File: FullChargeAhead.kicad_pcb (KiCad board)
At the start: 2 copper layers, 27.2 x 15.2 mm, 13 parts, among them P1 USB_PWR, P2 BATT, U1 MCP73834-FCI/UN

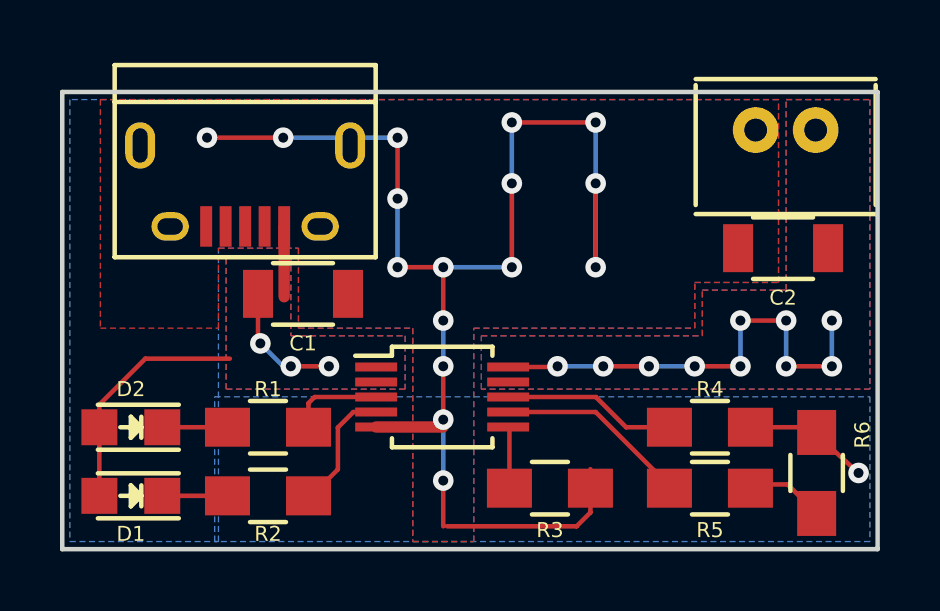
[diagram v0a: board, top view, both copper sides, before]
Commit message: Fix USB footprint.
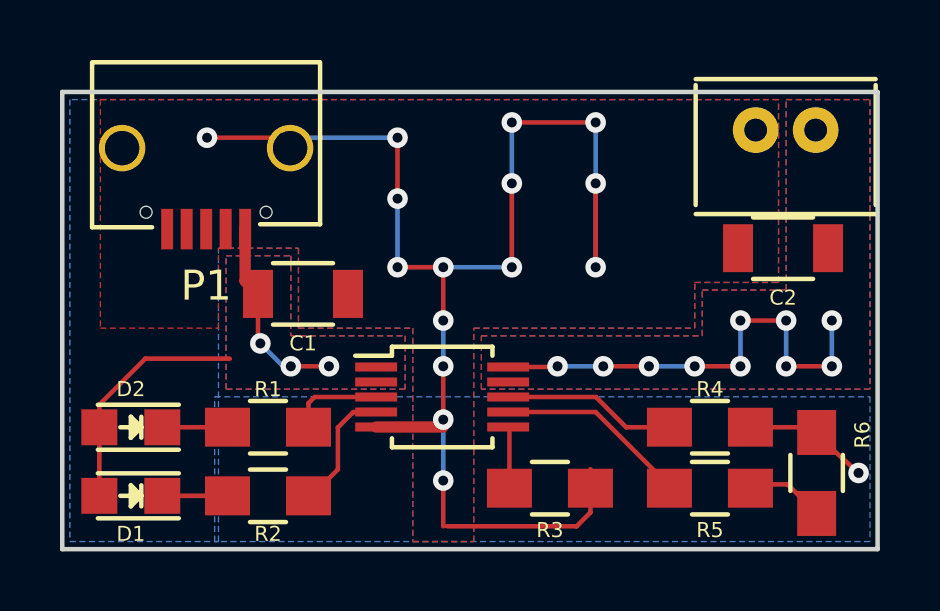
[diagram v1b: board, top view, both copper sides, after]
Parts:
- P1: footprint Connect:USB_Micro-B -> gl:USB_Micro-B-ebay
- moved P1 2.63 mm to (153.4, 104.5)
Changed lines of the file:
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@@
-(kicad_pcb (version 4) (host pcbnew 4.0.2+e4-6225~38~ubuntu16.04.1-stable)
+(kicad_pcb (version 4) (host pcbnew 4.0.3+e1-6302~38~ubuntu16.04.1-stable)
   (general
-    (links 27)
-    (no_connects 0)
+    (links 25)
+    (no_connects 3)
     (area 148.514999 99.238999 175.843001 114.629001)
     (thickness 1.6)
     (drawings 6)
-    (tracks 98)
+    (tracks 99)
     (zones 0)
     (modules 13)
@@
   )
   (setup
-    (last_trace_width 0.1524)
+    (last_trace_width 0.381)
     (user_trace_width 0.1524)
     (user_trace_width 0.381)
@@
     (pad_to_mask_clearance 0.2)
     (aux_axis_origin 0 0)
-    (visible_elements FFFEFF7F)
+    (visible_elements FFFFFF7F)
     (pcbplotparams
       (layerselection 0x00030_80000001)
@@
       (effects (font (size 0.5 0.5) (thickness 0.125)))
     )
-    (fp_text value 4.7u (at 0 2.3) (layer F.Fab)
+    (fp_text value 4.7u (at 0 0) (layer F.Fab)
       (effects (font (size 1 1) (thickness 0.15)))
     )
@@
       (effects (font (size 0.5 0.5) (thickness 0.125)))
     )
-    (fp_text value 4.7u (at 0 2.3 180) (layer F.Fab)
+    (fp_text value 4.7u (at -0.103 -0.127 180) (layer F.Fab)
       (effects (font (size 1 1) (thickness 0.15)))
     )
@@
       (effects (font (size 0.5 0.5) (thickness 0.125)))
     )
-    (fp_text value LED (at 0 1.75 180) (layer F.Fab)
+    (fp_text value LED (at 0 1.75 180) (layer F.Fab) hide
       (effects (font (size 1 1) (thickness 0.15)))
     )
@@
       (effects (font (size 0.5 0.5) (thickness 0.125)))
     )
-    (fp_text value LED (at 0 1.75 180) (layer F.Fab)
+    (fp_text value LED (at 0 1.75 180) (layer F.Fab) hide
       (effects (font (size 1 1) (thickness 0.15)))
     )
@@
     )
   )
-  (module Connect:USB_Micro-B (layer F.Cu)
-    (at 154.686 102.235 180)
-    (descr "Micro USB Type B Receptacle")
-    (tags "USB USB_B USB_micro USB_OTG")
-    (attr smd)
-    (fp_text reference P1 (at 2.032 -3.683 180) (layer F.SilkS) hide
-      (effects (font (size 1 1) (thickness 0.15)))
-    )
-    (fp_text value USB_PWR (at 0 4.8 180) (layer F.Fab)
-      (effects (font (size 1 1) (thickness 0.15)))
-    )
-    (fp_line (start -4.6 -2.8) (end 4.6 -2.8) (layer F.CrtYd) (width 0.05))
-    (fp_line (start 4.6 -2.8) (end 4.6 4.05) (layer F.CrtYd) (width 0.05))
-    (fp_line (start 4.6 4.05) (end -4.6 4.05) (layer F.CrtYd) (width 0.05))
-    (fp_line (start -4.6 4.05) (end -4.6 -2.8) (layer F.CrtYd) (width 0.05))
-    (fp_line (start -4.3509 3.81746) (end 4.3491 3.81746) (layer F.SilkS) (width 0.15))
-    (fp_line (start -4.3509 -2.58754) (end 4.3491 -2.58754) (layer F.SilkS) (width 0.15))
-    (fp_line (start 4.3491 -2.58754) (end 4.3491 3.81746) (layer F.SilkS) (width 0.15))
-    (fp_line (start 4.3491 2.58746) (end -4.3509 2.58746) (layer F.SilkS) (width 0.15))
-    (fp_line (start -4.3509 3.81746) (end -4.3509 -2.58754) (layer F.SilkS) (width 0.15))
-    (pad 1 smd rect (at -1.3009 -1.56254 270) (size 1.35 0.4) (layers F.Cu F.Paste F.Mask)
-      (net 12 /Vin))
-    (pad 2 smd rect (at -0.6509 -1.56254 270) (size 1.35 0.4) (layers F.Cu F.Paste F.Mask)
-      (net 4 "Net-(P1-Pad2)"))
-    (pad 3 smd rect (at -0.0009 -1.56254 270) (size 1.35 0.4) (layers F.Cu F.Paste F.Mask)
-      (net 5 "Net-(P1-Pad3)"))
-    (pad 4 smd rect (at 0.6491 -1.56254 270) (size 1.35 0.4) (layers F.Cu F.Paste F.Mask)
-      (net 6 "Net-(P1-Pad4)"))
-    (pad 5 smd rect (at 1.2991 -1.56254 270) (size 1.35 0.4) (layers F.Cu F.Paste F.Mask)
-      (net 1 GND))
-    (pad 6 thru_hole oval (at -2.5009 -1.56254 270) (size 0.95 1.25) (drill oval 0.55 0.85) (layers *.Cu *.Mask F.SilkS)
-      (net 1 GND))
-    (pad 6 thru_hole oval (at 2.4991 -1.56254 270) (size 0.95 1.25) (drill oval 0.55 0.85) (layers *.Cu *.Mask F.SilkS)
-      (net 1 GND))
-    (pad 6 thru_hole oval (at -3.5009 1.13746 270) (size 1.55 1) (drill oval 1.15 0.5) (layers *.Cu *.Mask F.SilkS)
-      (net 1 GND))
-    (pad 6 thru_hole oval (at 3.4991 1.13746 270) (size 1.55 1) (drill oval 1.15 0.5) (layers *.Cu *.Mask F.SilkS)
-      (net 1 GND))
-  )
   (module Resistors_SMD:R_0805_HandSoldering (layer F.Cu)
     (at 155.448 110.49 180)
@@
       (effects (font (size 0.5 0.5) (thickness 0.125)))
     )
-    (fp_text value 470 (at 0 2.1 180) (layer F.Fab)
+    (fp_text value 470 (at 0 0 180) (layer F.Fab)
       (effects (font (size 1 1) (thickness 0.15)))
     )
@@
       (effects (font (size 0.5 0.5) (thickness 0.125)))
     )
-    (fp_text value 470 (at 0 2.1 180) (layer F.Fab)
+    (fp_text value 470 (at 0 0 180) (layer F.Fab)
       (effects (font (size 1 1) (thickness 0.15)))
     )
@@
       (effects (font (size 0.5 0.5) (thickness 0.125)))
     )
-    (fp_text value 2k (at 0 2.1) (layer F.Fab)
+    (fp_text value 2k (at 0 0) (layer F.Fab)
       (effects (font (size 1 1) (thickness 0.15)))
     )
@@
       (effects (font (size 0.5 0.5) (thickness 0.125)))
     )
-    (fp_text value 10k (at 0 2.1) (layer F.Fab)
+    (fp_text value 10k (at 0 0) (layer F.Fab)
       (effects (font (size 1 1) (thickness 0.15)))
     )
@@
       (effects (font (size 0.5 0.5) (thickness 0.125)))
     )
-    (fp_text value 1k (at 0 2.1) (layer F.Fab)
+    (fp_text value 1k (at 0 0) (layer F.Fab)
       (effects (font (size 1 1) (thickness 0.15)))
     )
@@
       (effects (font (size 1 1) (thickness 0.15)))
     )
-    (fp_text value MCP73834-FCI/UN (at 0 2.6) (layer F.Fab)
+    (fp_text value MCP73834-FCI/UN (at 0 2.6) (layer F.Fab) hide
       (effects (font (size 1 1) (thickness 0.15)))
     )
@@
       (effects (font (size 0.5 0.5) (thickness 0.125)))
     )
-    (fp_text value R (at 0 2.1 90) (layer F.Fab)
+    (fp_text value R (at 0 0.127 90) (layer F.Fab)
       (effects (font (size 1 1) (thickness 0.15)))
     )
@@
     (pad 2 thru_hole circle (at 1 0 180) (size 1.524 1.524) (drill 0.762) (layers *.Cu *.Mask F.SilkS)
       (net 1 GND))
+  )
+  (module gl:USB_Micro-B-ebay (layer F.Cu)
+    (at 153.3851 104.52346 180)
+    (descr "Micro USB Type B Receptacle")
+    (tags "USB USB_B USB_micro USB_OTG")
+    (attr smd)
+    (fp_text reference P1 (at 0 -1.25 180) (layer F.SilkS)
+      (effects (font (size 1 1) (thickness 0.15)))
+    )
+    (fp_text value USB_PWR (at 0 7 180) (layer F.Fab)
+      (effects (font (size 1 1) (thickness 0.15)))
+    )
+    (fp_line (start -4.6 -0.6) (end 4.6 -0.6) (layer F.CrtYd) (width 0.05))
+    (fp_line (start 4.6 -0.6) (end 4.6 6.25) (layer F.CrtYd) (width 0.05))
+    (fp_line (start 4.6 6.25) (end -4.6 6.25) (layer F.CrtYd) (width 0.05))
+    (fp_line (start -4.6 6.25) (end -4.6 -0.6) (layer F.CrtYd) (width 0.05))
+    (fp_line (start -3.75 6.2) (end 3.75 6.2) (layer F.SilkS) (width 0.15))
+    (fp_line (start 3.8 0.7) (end 3.8 6.2) (layer F.SilkS) (width 0.15))
+    (fp_line (start -3.8 6.2) (end -3.8 0.8) (layer F.SilkS) (width 0.15))
+    (fp_line (start -3.8 0.8) (end -1.8 0.8) (layer F.SilkS) (width 0.15))
+    (fp_line (start 1.8 0.7) (end 3.8 0.7) (layer F.SilkS) (width 0.15))
+    (pad 1 smd rect (at -1.3009 0.63746 270) (size 1.35 0.4) (layers F.Cu F.Paste F.Mask)
+      (net 12 /Vin))
+    (pad 2 smd rect (at -0.6509 0.63746 270) (size 1.35 0.4) (layers F.Cu F.Paste F.Mask)
+      (net 4 "Net-(P1-Pad2)"))
+    (pad 3 smd rect (at -0.0009 0.63746 270) (size 1.35 0.4) (layers F.Cu F.Paste F.Mask)
+      (net 5 "Net-(P1-Pad3)"))
+    (pad 4 smd rect (at 0.6491 0.63746 270) (size 1.35 0.4) (layers F.Cu F.Paste F.Mask)
+      (net 6 "Net-(P1-Pad4)"))
+    (pad 5 smd rect (at 1.2991 0.63746 270) (size 1.35 0.4) (layers F.Cu F.Paste F.Mask)
+      (net 1 GND))
+    (pad "" np_thru_hole circle (at -2 1.2 270) (size 0.4 0.4) (drill 0.4) (layers *.Cu *.Mask F.SilkS))
+    (pad 6 thru_hole circle (at -2.8 3.33746 270) (size 1.55 1.55) (drill 1.15) (layers *.Cu *.Mask F.SilkS)
+      (net 1 GND))
+    (pad 6 thru_hole circle (at 2.8 3.33746 270) (size 1.55 1.55) (drill 1.15) (layers *.Cu *.Mask F.SilkS)
+      (net 1 GND))
+    (pad "" np_thru_hole circle (at 2 1.2 270) (size 0.4 0.4) (drill 0.4) (layers *.Cu *.Mask F.SilkS))
   )
   (gr_text v1 (at 151.384 107.442) (layer B.SilkS)
@@
   (segment (start 168.783 112.395) (end 166.37 109.982) (width 0.1524) (layer F.Cu) (net 11))
   (segment (start 166.37 109.982) (end 163.454523 109.982) (width 0.1524) (layer F.Cu) (net 11))
+  (segment (start 154.686 103.886) (end 154.686 105.616) (width 0.381) (layer F.Cu) (net 12))
+  (segment (start 154.686 105.616) (end 155.115 106.045) (width 0.381) (layer F.Cu) (net 12))
   (segment (start 151.36114 108.204) (end 154.178 108.204) (width 0.1524) (layer F.Cu) (net 12))
   (segment (start 149.82698 110.49) (end 149.82698 109.73816) (width 0.1524) (layer F.Cu) (net 12))
@@
   (via (at 155.194 107.696) (size 0.6858) (drill 0.3302) (layers F.Cu B.Cu) (net 12))
   (segment (start 155.115 107.617) (end 155.194 107.696) (width 0.1524) (layer F.Cu) (net 12))
-  (segment (start 155.9869 103.79754) (end 155.9869 106.1411) (width 0.381) (layer F.Cu) (net 12))
   (segment (start 163.454523 108.482) (end 165.076 108.482) (width 0.1524) (layer F.Cu) (net 13))
   (via (at 174.244 106.934) (size 0.6858) (drill 0.3302) (layers F.Cu B.Cu) (net 13))
